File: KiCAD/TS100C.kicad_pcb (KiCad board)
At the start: 4 copper layers, 84 x 10 mm, 63 parts, among them J1 USB_C_Receptacle_USB2.0, J2 OLED_64x32, J3 A, J4 B, J5 DNP, P1 TC2030-CTX, Q1 SS8050, Q2 DMP3017SFG, SW1 key1, SW2 key2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

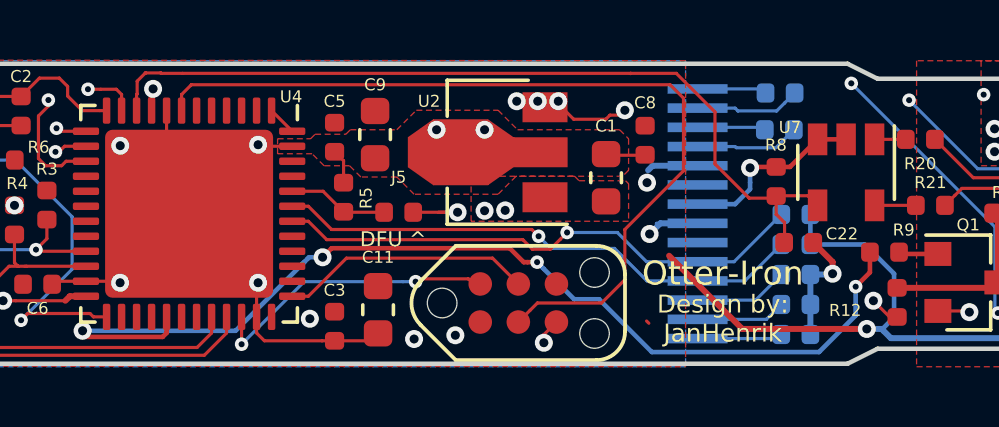
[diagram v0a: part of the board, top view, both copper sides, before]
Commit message: optimized TC & Display connector, added pullup
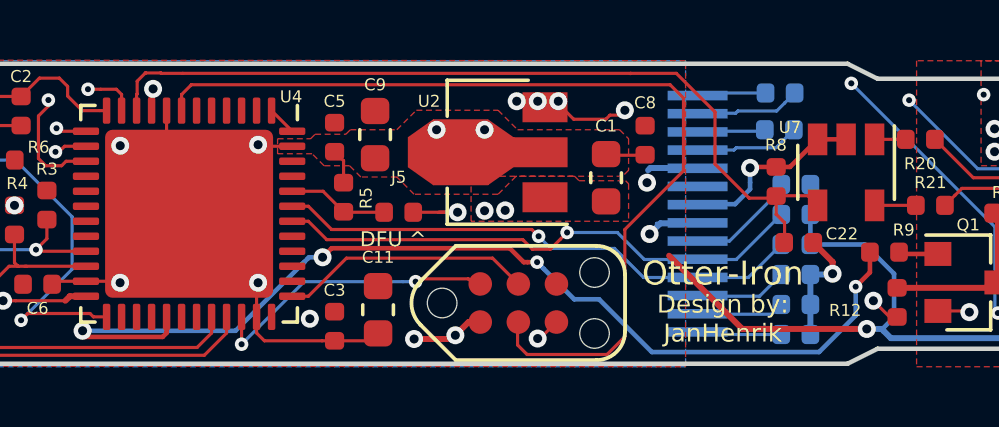
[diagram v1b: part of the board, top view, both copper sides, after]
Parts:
- added R24: 2k37, Resistor_SMD:R_0402_1005Metric, B.Cu at (128.3, 84.0)
- C19, C20: value 0.1μF -> 1μF 25V
- U3: value STUSB4500 -> STUSB4500QTR
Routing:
- net Net-(J2-Pad9): track 0.00 -> 3.66 mm
- net nRST: track 28.6 -> 31.2 mm
- net +3V3: track 77.1 -> 79.1 mm
